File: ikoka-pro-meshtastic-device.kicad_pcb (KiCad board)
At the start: 2 copper layers, 80 x 100 mm, 67 parts, among them J1 Barrel_Jack_Switch, J10 BWSMA-KWE-Z001, J2 Conn_ARM_JTAG_SWD_10, J3 BWSMA-KWE-Z001, J4 Conn_01x01, J5 Conn_01x01, J6 Conn_01x01, J7 Conn_01x01, J8 USB_C_Receptacle_USB2.0_16P, J9 SM04B-SRSS-TB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

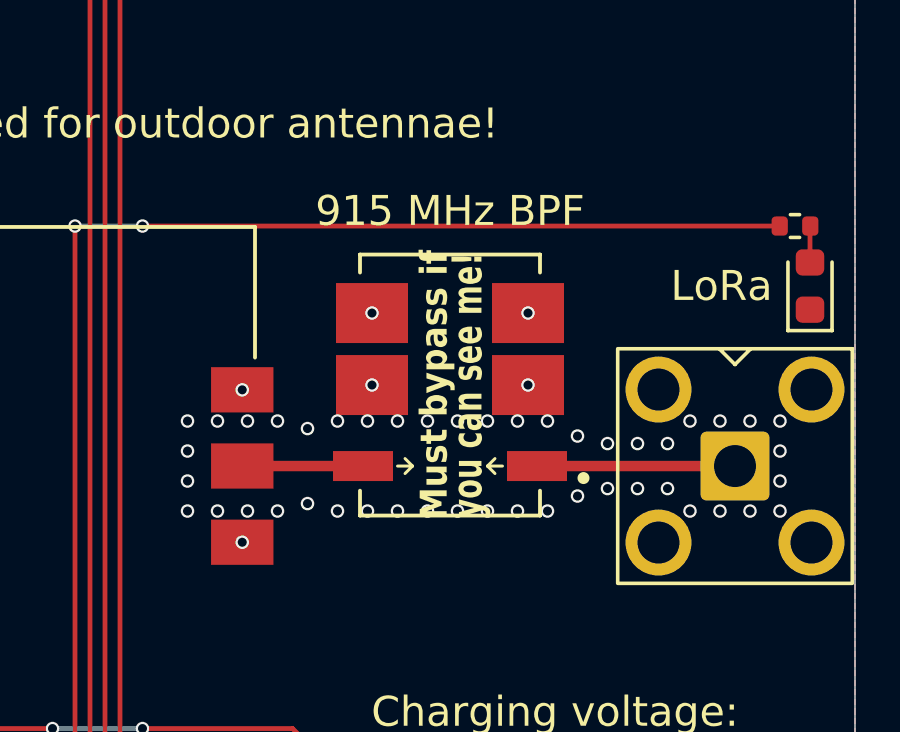
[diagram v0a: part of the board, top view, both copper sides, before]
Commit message: fix(pcbnew): Redraw footprint for Taoglas DBP.915.V.A.30 (fixes #4)
- Silkscreen re-drawn following KLC guidelines and correctly aligned to part
- Courtyard re-drawn following KLC guidelines and correctly aligned to part
- Use 0.25mm roundrects for pads
- Remove custom soldermask and paste in favor of KiCad pad defaults

Signed-off-by: Andrew Yong <me@ndoo.sg>
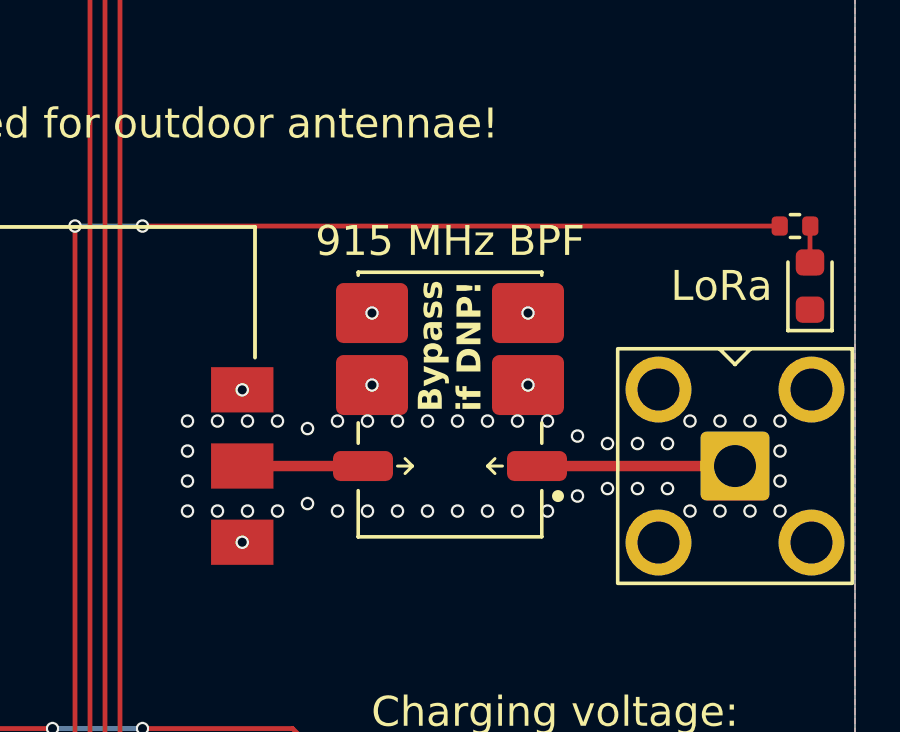
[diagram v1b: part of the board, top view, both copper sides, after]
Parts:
- moved FL1 2.70 mm to (176.5, 80.0)
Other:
- board text added: "Bypass if DNP!"
- board text removed: "Must bypass if"
- board text removed: "you can see me!"

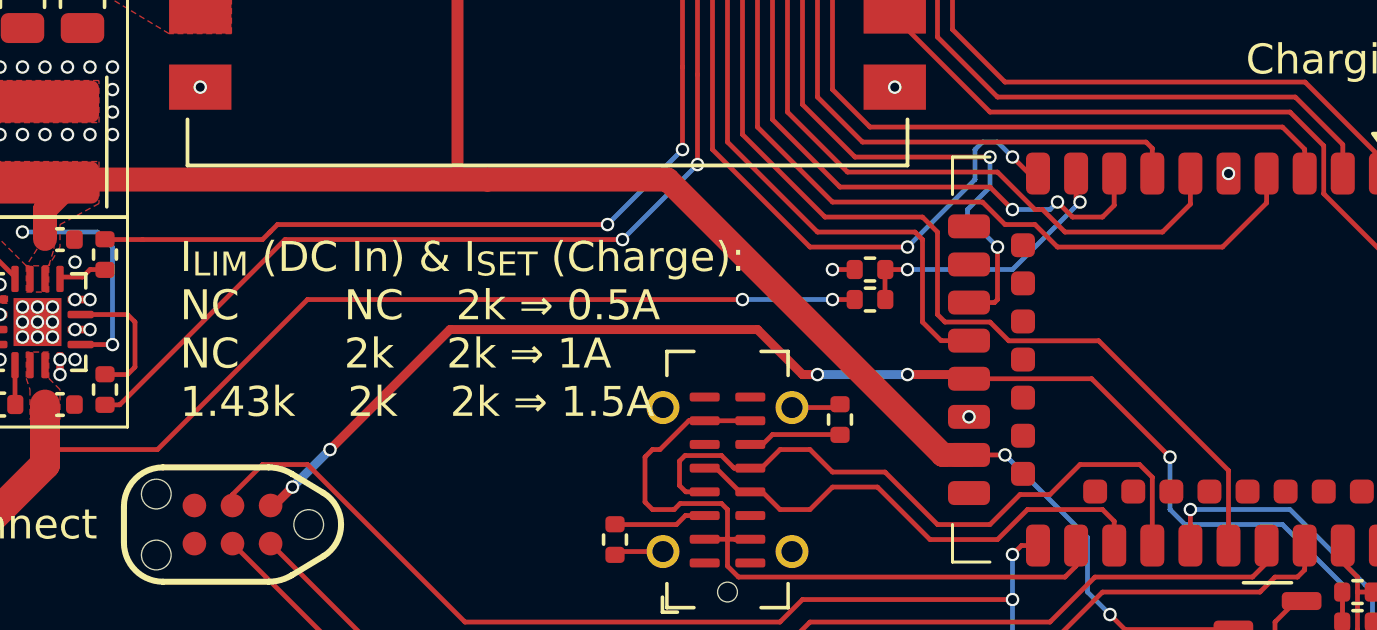
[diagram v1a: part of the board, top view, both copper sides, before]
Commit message: fix: Use correct resistor values for ILIM and default to 1.5A (fixes #7)
Signed-off-by: Andrew Yong <me@ndoo.sg>
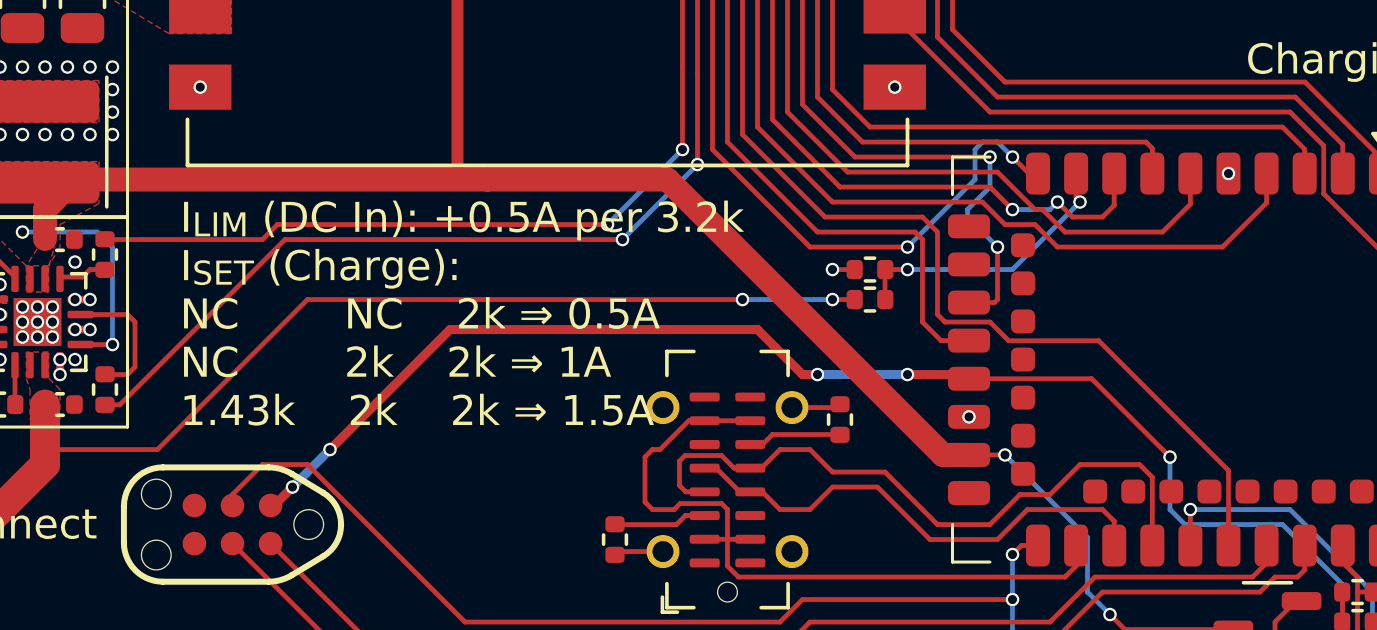
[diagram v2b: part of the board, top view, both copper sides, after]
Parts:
- R18: value 1.43k -> 3.3k
- R7, R8: value 2k -> 3.3k
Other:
- board text added: "I_{LIM} (DC In): +0.5A per 3.2k I_{SET} (Charge): NC NC 2k ⇒ 0.5A NC 2k 2k ⇒ 1A 1.43k 2k 2k ⇒ 1.5A"
- board text removed: "I_{LIM} (DC In) & I_{SET} (Charge): NC NC 2k ⇒ 0.5A NC 2k 2k ⇒ 1A 1.43k 2k 2k ⇒ 1.5A"

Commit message: fix: Change USB-C CC resistors from 510Ω to 5.1kΩ (fixes #8)
Signed-off-by: Andrew Yong <me@ndoo.sg>
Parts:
- R20, R21: value 510 -> 5.1k
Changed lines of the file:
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@@
 			)
 		)
-		(property "Value" "510"
+		(property "Value" "5.1k"
 			(at 0 1.17 90)
 			(layer "F.Fab")
@@
 			)
 		)
-		(property "LCSC" "C25123"
+		(property "LCSC" "C25905"
 			(at 0 0 0)
 			(layer "F.SilkS")
@@
 			)
 		)
-		(property "Value" "510"
+		(property "Value" "5.1k"
 			(at 0 1.17 90)
 			(layer "F.Fab")
@@
 			)
 		)
-		(property "LCSC" "C25123"
+		(property "LCSC" "C25905"
 			(at 0 0 0)
 			(layer "F.SilkS")

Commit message: chore: v1.0.0 silkscreen
Signed-off-by: Andrew Yong <me@ndoo.sg>
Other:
- board text added: "v1.0.0"
- board text removed: "v0.9.0"
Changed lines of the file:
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@@
 		)
 	)
-	(gr_text "v0.9.0"
+	(gr_text "v1.0.0"
 		(locked yes)
 		(at 145.5 56 0)
@@
 			(justify left bottom)
 		)
-		(render_cache "v0.9.0" 0
+		(render_cache "v1.0.0" 0
 			(polygon
 				(pts
@@
 			(polygon
 				(pts
-					(xy 146.747116 54.772867) (xy 146.798639 54.78983) (xy 146.845693 54.816658) (xy 146.887848 54.851868)
-					(xy 146.924603 54.893962) (xy 146.957091 54.943642) (xy 146.984236 54.997697) (xy 147.006734 55.056055)
-					(xy 147.024114 55.116761) (xy 147.03647 55.179703) (xy 147.043877 55.243181) (xy 147.046301 55.304389)
-					(xy 147.04421 55.367582) (xy 147.037875 55.431945) (xy 147.026983 55.495461) (xy 147.011313 55.555898)
-					(xy 146.990451 55.613916) (xy 146.964785 55.667639) (xy 146.933356 55.716832) (xy 146.896946 55.758375)
-					(xy 146.854494 55.792793) (xy 146.805661 55.819314) (xy 146.751689 55.835938) (xy 146.689584 55.841723)
-					(xy 146.631991 55.835911) (xy 146.580408 55.818948) (xy 146.533401 55.792136) (xy 146.491259 55.756971)
-					(xy 146.454534 55.714844) (xy 146.422016 55.665197) (xy 146.394855 55.611092) (xy 146.372313 55.552723)
-					(xy 146.354954 55.49207) (xy 146.342576 55.429441) (xy 146.335226 55.366193) (xy 146.332807 55.304389)
-					(xy 146.333812 55.273797) (xy 146.477581 55.273797) (xy 146.48039 55.363496) (xy 146.491564 55.462048)
-					(xy 146.515012 55.558096) (xy 146.532581 55.602546) (xy 146.554152 55.640772) (xy 146.581166 55.673599)
-					(xy 146.612953 55.69878) (xy 146.650035 55.714921) (xy 146.695141 55.720579) (xy 146.735917 55.716259)
-					(xy 146.769635 55.704031) (xy 146.799244 55.684562) (xy 146.82459 55.65903) (xy 146.845343 55.628626)
-					(xy 146.862325 55.592901) (xy 146.885772 55.512301) (xy 146.897984 55.42364) (xy 146.901526 55.334309)
-					(xy 146.898717 55.24461) (xy 146.887482 55.146425) (xy 146.864096 55.050376) (xy 146.846476 55.005672)
-					(xy 146.824895 54.9677) (xy 146.797951 54.935127) (xy 146.766154 54.909998) (xy 146.729073 54.893857)
-					(xy 146.683967 54.888199) (xy 146.643182 54.892517) (xy 146.609412 54.904747) (xy 146.579832 54.924154)
-					(xy 146.554518 54.949443) (xy 146.533797 54.979551) (xy 146.516721 55.015572) (xy 146.493335 55.096477)
-					(xy 146.481062 55.184771) (xy 146.477581 55.273797) (xy 146.333812 55.273797) (xy 146.334883 55.241203)
-					(xy 146.341172 55.176894) (xy 146.352111 55.113324) (xy 146.367794 55.05288) (xy 146.388656 54.994861)
-					(xy 146.414323 54.941139) (xy 146.445752 54.891946) (xy 146.482161 54.850403) (xy 146.524555 54.815963)
-					(xy 146.57308 54.789464) (xy 146.626836 54.772866) (xy 146.689584 54.767055)
+					(xy 146.514706 55.83) (xy 146.514706 55.716671) (xy 146.686043 55.716671) (xy 146.686043 55.042194)
+					(xy 146.726648 54.883681) (xy 146.631516 55.013557) (xy 146.483199 55.144776) (xy 146.407667 55.060329)
+					(xy 146.728053 54.767055) (xy 146.832955 54.781038) (xy 146.832955 55.716671) (xy 147.004352 55.716671)
+					(xy 147.004352 55.83)
 				)
 			)
@@
 			(polygon
 				(pts
-					(xy 148.098191 54.772756) (xy 148.154309 54.788792) (xy 148.204699 54.814289) (xy 148.246999 54.84625)
-					(xy 148.282941 54.884588) (xy 148.312395 54.928194) (xy 148.336057 54.975409) (xy 148.354344 55.024181)
-					(xy 148.367892 55.074038) (xy 148.376753 55.122978) (xy 148.383408 55.213286) (xy 148.379263 55.294437)
-					(xy 148.366983 55.372349) (xy 148.346581 55.447664) (xy 148.318684 55.518101) (xy 148.283181 55.584199)
-					(xy 148.24071 55.644558) (xy 148.191196 55.69857) (xy 148.13538 55.744698) (xy 148.073487 55.782689)
-					(xy 148.004588 55.812658) (xy 147.931043 55.832586) (xy 147.85102 55.841723) (xy 147.829344 55.728394)
-					(xy 147.884468 55.721998) (xy 147.936879 55.708598) (xy 147.987063 55.688155) (xy 148.056516 55.646214)
-					(xy 148.117184 55.592473) (xy 148.167811 55.528279) (xy 148.208164 55.453316) (xy 148.227844 55.399426)
-					(xy 148.241029 55.342928) (xy 148.24767 55.283384) (xy 148.191739 55.364839) (xy 148.149521 55.39315)
-					(xy 148.108818 55.412161) (xy 148.065458 55.423493) (xy 148.014724 55.427487) (xy 147.947901 55.421707)
-					(xy 147.886741 55.404773) (xy 147.830828 55.377025) (xy 147.783182 55.340048) (xy 147.744088 55.2941)
-					(xy 147.713939 55.238932) (xy 147.695267 55.177422) (xy 147.688782 55.107041) (xy 147.689849 55.094462)
-					(xy 147.831481 55.094462) (xy 147.834443 55.139299) (xy 147.843021 55.179825) (xy 147.85775 55.217057)
-					(xy 147.878009 55.248213) (xy 147.904367 55.273847) (xy 147.937482 55.293703) (xy 147.975522 55.305907)
-					(xy 148.021746 55.310251) (xy 148.058156 55.307238) (xy 148.092759 55.298283) (xy 148.125441 55.284169)
-					(xy 148.155041 55.266165) (xy 148.181732 55.244376) (xy 148.20505 55.21927) (xy 148.224555 55.191422)
-					(xy 148.239305 55.162178) (xy 148.234393 55.109868) (xy 148.223918 55.059535) (xy 148.20756 55.011881)
-					(xy 148.186121 54.970692) (xy 148.158241 54.935268) (xy 148.124206 54.907922) (xy 148.0843 54.890393)
-					(xy 148.036461 54.884291) (xy 147.990531 54.888317) (xy 147.951099 54.899801) (xy 147.915853 54.91849)
-					(xy 147.886741 54.942848) (xy 147.863433 54.972841) (xy 147.84583 55.00916) (xy 147.835173 55.049252)
-					(xy 147.831481 55.094462) (xy 147.689849 55.094462) (xy 147.694997 55.033784) (xy 147.712901 54.969288)
-					(xy 147.742312 54.910945) (xy 147.781411 54.861882) (xy 147.830118 54.822096) (xy 147.889183 54.791906)
-					(xy 147.955018 54.773487) (xy 148.030844 54.767055)
+					(xy 148.075797 54.772867) (xy 148.12732 54.78983) (xy 148.174374 54.816658) (xy 148.21653 54.851868)
+					(xy 148.253284 54.893962) (xy 148.285772 54.943642) (xy 148.312917 54.997697) (xy 148.335415 55.056055)
+					(xy 148.352795 55.116761) (xy 148.365151 55.179703) (xy 148.372558 55.243181) (xy 148.374982 55.304389)
+					(xy 148.372891 55.367582) (xy 148.366556 55.431945) (xy 148.355664 55.495461) (xy 148.339994 55.555898)
+					(xy 148.319132 55.613916) (xy 148.293466 55.667639) (xy 148.262037 55.716832) (xy 148.225628 55.758375)
+					(xy 148.183175 55.792793) (xy 148.134342 55.819314) (xy 148.08037 55.835938) (xy 148.018265 55.841723)
+					(xy 147.960672 55.835911) (xy 147.909089 55.818948) (xy 147.862082 55.792136) (xy 147.81994 55.756971)
+					(xy 147.783215 55.714844) (xy 147.750697 55.665197) (xy 147.723536 55.611092) (xy 147.700994 55.552723)
+					(xy 147.683635 55.49207) (xy 147.671257 55.429441) (xy 147.663907 55.366193) (xy 147.661488 55.304389)
+					(xy 147.662493 55.273797) (xy 147.806263 55.273797) (xy 147.809071 55.363496) (xy 147.820245 55.462048)
+					(xy 147.843693 55.558096) (xy 147.861262 55.602546) (xy 147.882833 55.640772) (xy 147.909847 55.673599)
+					(xy 147.941634 55.69878) (xy 147.978716 55.714921) (xy 148.023822 55.720579) (xy 148.064598 55.716259)
+					(xy 148.098316 55.704031) (xy 148.127925 55.684562) (xy 148.153271 55.65903) (xy 148.174024 55.628626)
+					(xy 148.191006 55.592901) (xy 148.214453 55.512301) (xy 148.226666 55.42364) (xy 148.230207 55.334309)
+					(xy 148.227398 55.24461) (xy 148.216163 55.146425) (xy 148.192777 55.050376) (xy 148.175158 55.005672)
+					(xy 148.153576 54.9677) (xy 148.126632 54.935127) (xy 148.094836 54.909998) (xy 148.057754 54.893857)
+					(xy 148.012648 54.888199) (xy 147.971863 54.892517) (xy 147.938093 54.904747) (xy 147.908513 54.924154)
+					(xy 147.883199 54.949443) (xy 147.862478 54.979551) (xy 147.845403 55.015572) (xy 147.822016 55.096477)
+					(xy 147.809743 55.184771) (xy 147.806263 55.273797) (xy 147.662493 55.273797) (xy 147.663564 55.241203)
+					(xy 147.669853 55.176894) (xy 147.680792 55.113324) (xy 147.696475 55.05288) (xy 147.717337 54.994861)
+					(xy 147.743004 54.941139) (xy 147.774433 54.891946) (xy 147.810842 54.850403) (xy 147.853236 54.815963)
+					(xy 147.901762 54.789464) (xy 147.955517 54.772866) (xy 148.018265 54.767055)
 				)
 			)
